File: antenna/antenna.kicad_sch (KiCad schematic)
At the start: 17 parts, among them J1 Conn_01x05_Pin, J2 Conn_01x05_Pin, J3 Conn_01x05_Pin, J5 USB_C_Receptacle, U1 ESP32-C3-WROOM-02, U2 AMS1117-3.3

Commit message: great success!
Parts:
- removed JP1: SolderJumper_2_Open, Jumper:SolderJumper-2_P1.3mm_Open_RoundedPad1.0x1.5mm, symbol Jumper:SolderJumper_2_Open
- added C6: 4u7F, Capacitor_SMD:C_0805_2012Metric_Pad1.18x1.45mm_HandSolder, symbol Device:C_Small
- added R1: 10k, Resistor_SMD:R_0805_2012Metric_Pad1.20x1.40mm_HandSolder, symbol Device:R_Small
- added R2: 10k, Resistor_SMD:R_0805_2012Metric_Pad1.20x1.40mm_HandSolder, symbol Device:R
- added SW1: SW_Push, 0_NRD_footprints:SW_PUSH-12mm_Wuerth-430456085736, symbol Switch:SW_Push
- added SW2: SW_Push, Button_Switch_SMD:SW_Tactile_SPST_NO_Straight_CK_PTS636Sx25SMTRLFS, symbol Switch:SW_Push
- C1: value C -> 4u7F
- C2: value 100nF -> 4u7F
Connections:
- net GND: now also C6.2, SW1.1, SW2.1
- net at C2.1, C3.1, U1.1 (3V3)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: now also R1.2, R2.2
- net at U1.16 (IO2): now also D1.2 (DIN), J1.3 (Pin_3)
- net at U1.2 (EN): now also C6.1, R1.1
- net at U1.7 (IO8): now also R2.1
- net at U1.8 (IO9): now also SW1.2
- new net: SW2.2, U1.18 (IO0)

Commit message: updated all coolness
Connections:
- net at SW1.2, U1.8 (IO9): now also J2.3 (Pin_3)
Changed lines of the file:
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@@
+	)
+	(junction
+		(at 138.43 53.34)
+		(diameter 0)
+		(color 0 0 0 0)
 	)
 	(junction
@@
 	(wire
 		(pts
+			(xy 138.43 160.02) (xy 138.43 53.34)
+		)
+		(stroke
+			(width 0)
+			(type default)
+		)
+	)
+	(wire
+		(pts
 			(xy 138.43 20.32) (xy 133.35 20.32)
 		)
@@
 	(wire
 		(pts
+			(xy 82.55 160.02) (xy 138.43 160.02)
+		)
+		(stroke
+			(width 0)
+			(type default)
+		)
+	)
+	(wire
+		(pts
 			(xy 104.14 20.32) (xy 100.33 20.32)
 		)
@@
 	(wire
 		(pts
+			(xy 74.93 168.91) (xy 82.55 168.91)
+		)
+		(stroke
+			(width 0)
+			(type default)
+		)
+	)
+	(wire
+		(pts
 			(xy 71.12 80.01) (xy 69.85 80.01)
 		)
@@
 		)
 		(stroke
+			(width 0)
+			(type default)
+		)
+	)
+	(wire
+		(pts
+			(xy 82.55 168.91) (xy 82.55 160.02)
+		)
+		(stroke

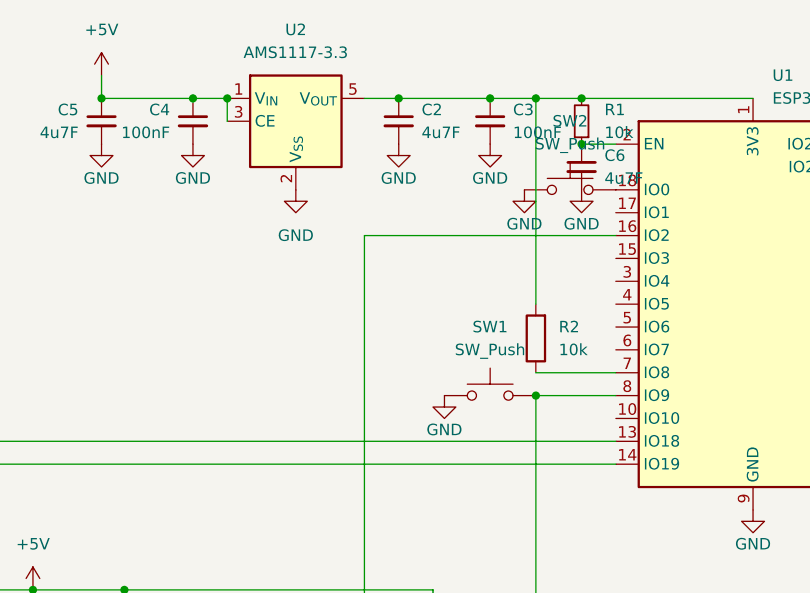
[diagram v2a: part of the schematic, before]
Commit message: added mic to antenna, decagons, octagons and all the shenanigans
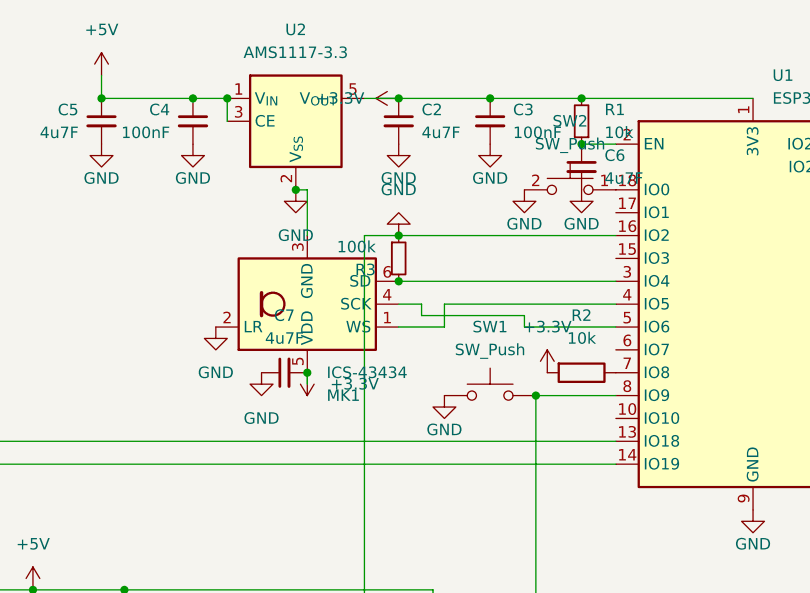
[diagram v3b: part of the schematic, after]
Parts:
- added C7: 4u7F, Capacitor_SMD:C_0805_2012Metric_Pad1.18x1.45mm_HandSolder, symbol Device:C_Small
- added MK1: ICS-43434, Sensor_Audio:InvenSense_ICS-43434-6_3.5x2.65mm, symbol Sensor_Audio:ICS-43434
- added R3: 100k, Resistor_SMD:R_0805_2012Metric_Pad1.20x1.40mm_HandSolder, symbol Device:R_Small
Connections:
- net GND: now also D1.2 (DIN), J1.3 (Pin_3), SW2.2, U1.16 (IO2), C7.1, MK1.2 (LR), MK1.3 (GND), R3.1; no longer SW2.1
- net +3.3V: now reaches C2.1, C3.1, R1.2, R2.2, U1.1 (3V3), U2.5 (V_{OUT})
- net +3.3V: now also C7.2, MK1.5 (VDD)
- net at U1.18 (IO0): now also SW2.1; no longer SW2.2
- net at U1.3 (IO4): now also MK1.6 (SD), R3.2
- net at U1.4 (IO5): now also MK1.1 (WS)
- net at U1.5 (IO6): now also MK1.4 (SCK)
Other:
- moved on the sheet: R2

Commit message: url-update and some bla
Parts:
- removed C7: 4u7F, Capacitor_SMD:C_0805_2012Metric_Pad1.18x1.45mm_HandSolder, symbol Device:C_Small
- removed MK1: ICS-43434, Sensor_Audio:InvenSense_ICS-43434-6_3.5x2.65mm, symbol Sensor_Audio:ICS-43434
- removed R3: 100k, Resistor_SMD:R_0805_2012Metric_Pad1.20x1.40mm_HandSolder, symbol Device:R_Small
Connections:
- net GND: now also SW2.1; no longer D1.2 (DIN), J1.3 (Pin_3), SW2.2, U1.16 (IO2)
- net at U1.18 (IO0): now also SW2.2; no longer SW2.1
- net +3.3V: no longer names the net of C2.1, C3.1, R1.2, R2.2, U1.1 (3V3), U2.5 (V_{OUT})
- new net: D1.2 (DIN), J1.3 (Pin_3), U1.16 (IO2)
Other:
- moved on the sheet: R2
